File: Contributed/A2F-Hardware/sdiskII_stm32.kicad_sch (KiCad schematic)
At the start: 33 parts, among them J1 SDISKII IN (CARD), J2 SDISKII OUT (DRIVE), J3 EA W128064-OLED (FPC31), J4 UART, U1 BlackPill STMF4X1, U2 DM-OLED096-636, U3 EA OLEDM128-6, U4 74x257

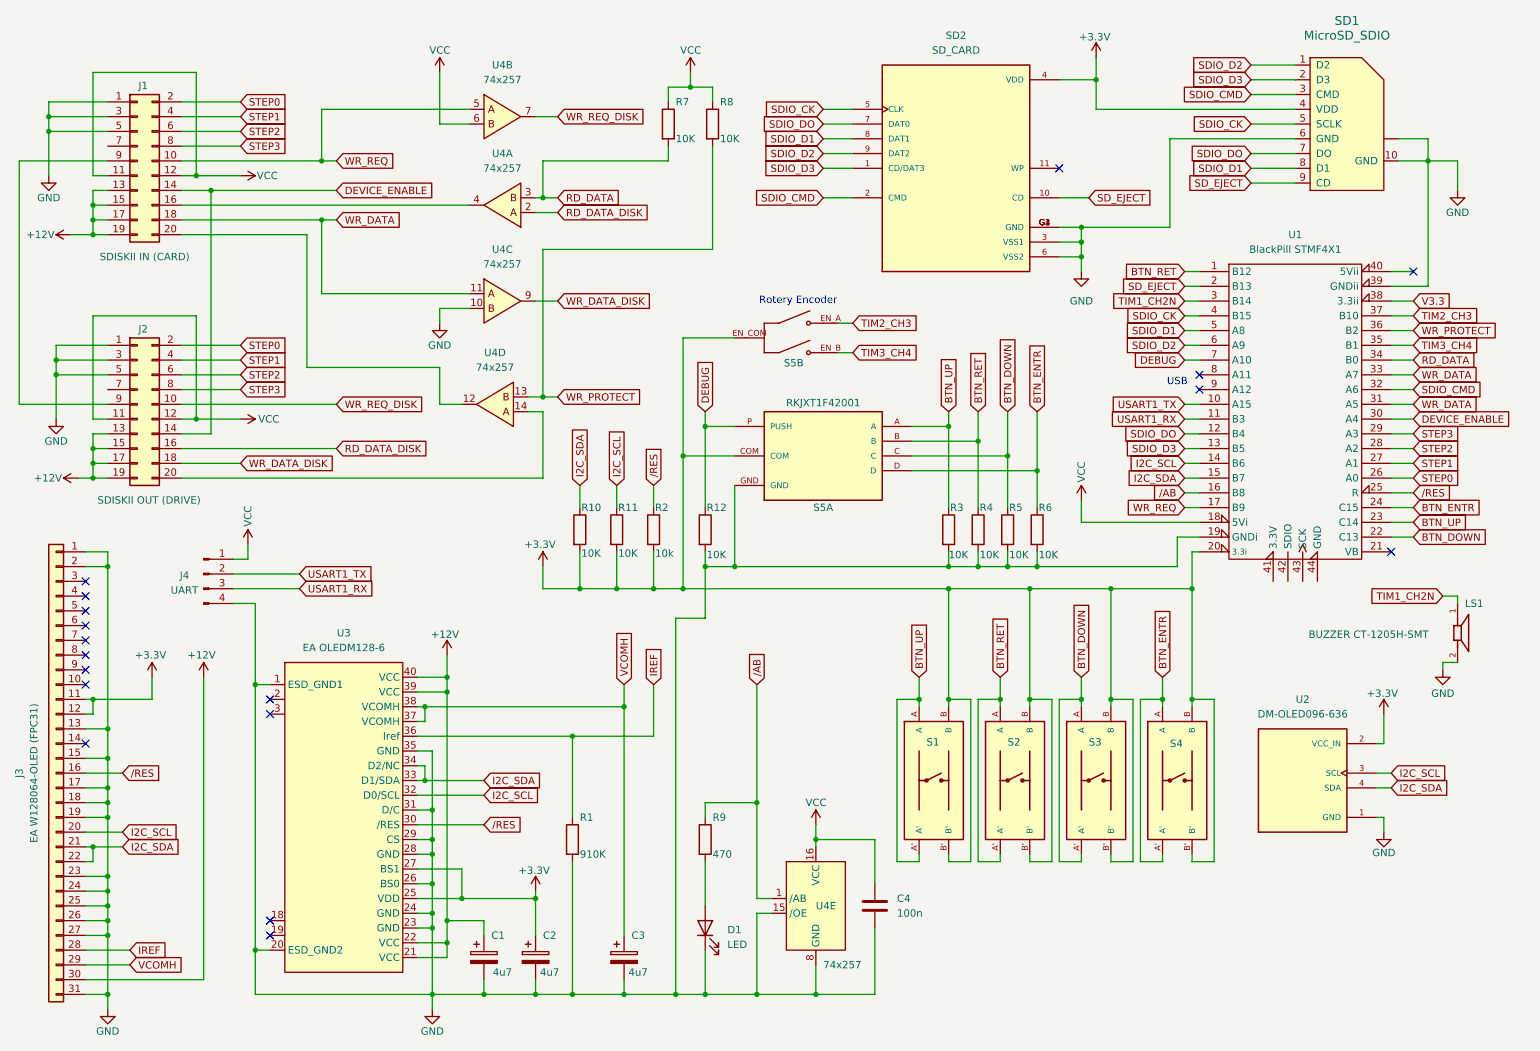
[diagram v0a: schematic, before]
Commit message: Initial upload
Rotary encoder support buggy
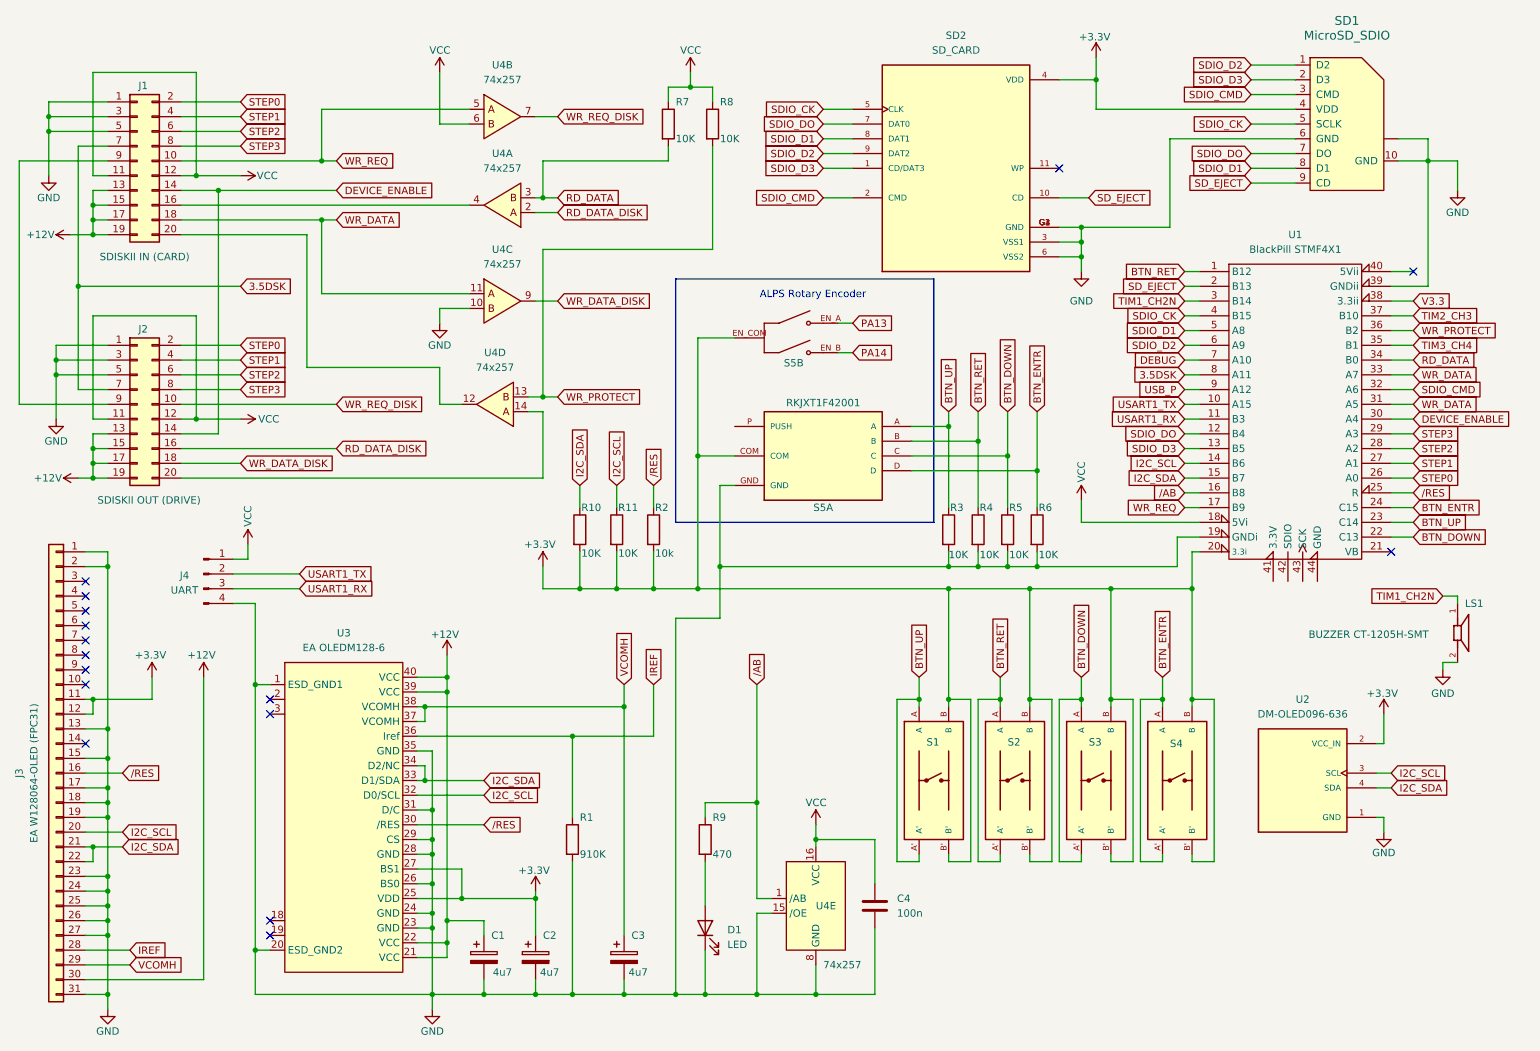
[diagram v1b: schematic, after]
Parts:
- removed R12: 10K, Resistor_SMD:R_0805_2012Metric_Pad1.20x1.40mm_HandSolder, symbol Device:R
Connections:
- net DEBUG: no longer S5.P (PUSH)
- net TIM2_CH3: no longer S5.EN_A
- net TIM3_CH4: no longer S5.EN_B
- net 3.5DSK: now reaches J1.7 (Pin_7)
- net 3.5DSK: now also J2.7 (Pin_7), U1.8 (A11)
- net USB_P: now reaches U1.9 (A12)
- new net PA13: S5.EN_A
- new net PA14: S5.EN_B
- no-connect marks 18 -> 16
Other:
- note added: "ALPS Rotary Encoder"
- note removed: "Rotery Encoder"
- note removed: "USB"

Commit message: RE update
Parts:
- added R12, R13: 10K, Resistor_SMD:R_0805_2012Metric_Pad1.20x1.40mm_HandSolder, symbol Device:R
- LS1: value BUZZER CT-1205H-SMT -> CT-1205H-SMT
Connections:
- net GND: now also R12.2, R13.2
- net PA13: now also U1.42 (SDIO), R12.1
- net PA14: now also U1.43 (SCK), R13.1
- no-connect marks 16 -> 18
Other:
- moved on the sheet: LS1

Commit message: Make Filsystem fixed
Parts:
- U1: footprint acheron_Hardware.pretty-master:Mini_F4X1_STM32_VIB -> sdisk_stm32:Mini_F4X1_STM32_VIB
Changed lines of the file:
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@@
 (kicad_sch
-	(version 20231120)
+	(version 20250114)
 	(generator "eeschema")
-	(generator_version "8.0")
+	(generator_version "9.0")
 	(paper "A4")
 	(title_block
@@
 		(rev "20")
 	)
+	(rectangle
+		(start 132.08 60.96)
+		(end 176.53 102.87)
+		(stroke
+			(width 0)
+			(type default)
+		)
+		(fill
+			(type none)
+		)
+	)
+	(text "ALPS Rotary Encoder"
+		(exclude_from_sim no)
+		(at 155.702 63.754 0)
+		(effects
+			(font
+				(size 1.27 1.27)
+			)
+		)
+	)
 	(junction
 		(at 207.01 114.3)
@@
 		)
 	)
-	(rectangle
-		(start 132.08 60.96)
-		(end 176.53 102.87)
-		(stroke
-			(width 0)
-			(type default)
-		)
-		(fill
-			(type none)
-		)
-	)
-	(text "ALPS Rotary Encoder"
-		(exclude_from_sim no)
-		(at 155.702 63.754 0)
-		(effects
-			(font
-				(size 1.27 1.27)
-			)
-		)
-	)
 	(global_label "USART1_RX"
 		(shape input)
@@
 			)
 		)
-		(property "Footprint" "acheron_Hardware.pretty-master:Mini_F4X1_STM32_VIB"
+		(property "Footprint" "sdisk_stm32:Mini_F4X1_STM32_VIB"
 			(at 240.792 127.254 0)
 			(effects
@@
 		)
 	)
+	(embedded_fonts no)
 )

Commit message: final v0.80.1
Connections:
- net BTN_ENTR: now also S5.P (PUSH)
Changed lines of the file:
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@@
 	)
 	(rectangle
-		(start 132.08 60.96)
-		(end 176.53 102.87)
+		(start 133.35 60.96)
+		(end 176.53 104.14)
 		(stroke
 			(width 0)
@@
 	)
 	(junction
+		(at 138.43 110.49)
+		(diameter 0)
+		(color 0 0 0 0)
+	)
+	(junction
 		(at 90.17 152.4)
 		(diameter 0)
@@
 	)
 	(junction
+		(at 173.99 93.98)
+		(diameter 0)
+		(color 0 0 0 0)
+	)
+	(junction
 		(at 31.75 50.8)
 		(diameter 0)
@@
 	)
 	(junction
-		(at 139.7 110.49)
-		(diameter 0)
-		(color 0 0 0 0)
-	)
-	(junction
 		(at 31.75 95.25)
 		(diameter 0)
@@
 	(wire
 		(pts
+			(xy 138.43 110.49) (xy 179.07 110.49)
+		)
+		(stroke
+			(width 0)
+			(type default)
+		)
+	)
+	(wire
+		(pts
 			(xy 179.07 161.29) (xy 179.07 160.02)
 		)
@@
 	(wire
 		(pts
-			(xy 139.7 96.52) (xy 142.24 96.52)
+			(xy 138.43 96.52) (xy 142.24 96.52)
 		)
 		(stroke
@@
 	(wire
 		(pts
-			(xy 172.72 93.98) (xy 194.31 93.98)
+			(xy 173.99 93.98) (xy 194.31 93.98)
+		)
+		(stroke
+			(width 0)
+			(type default)
+		)
+	)
+	(wire
+		(pts
+			(xy 172.72 93.98) (xy 173.99 93.98)
 		)
 		(stroke
@@
 	(wire
 		(pts
-			(xy 139.7 96.52) (xy 139.7 110.49)
+			(xy 138.43 96.52) (xy 138.43 110.49)
 		)
 		(stroke
@@
 	(wire
 		(pts
+			(xy 140.97 86.36) (xy 140.97 101.6)
+		)
+		(stroke
+			(width 0)
+			(type default)
+		)
+	)
+	(wire
+		(pts
 			(xy 255.27 90.17) (xy 259.08 90.17)
 		)
@@
 	(wire
 		(pts
-			(xy 215.9 133.35) (xy 215.9 134.62)
+			(xy 140.97 101.6) (xy 173.99 101.6)
 		)
 		(stroke
@@
 	(wire
 		(pts
-			(xy 220.98 107.95) (xy 220.98 114.3)
+			(xy 215.9 133.35) (xy 215.9 134.62)
 		)
 		(stroke
@@
 	(wire
 		(pts
-			(xy 31.75 87.63) (xy 31.75 90.17)
+			(xy 220.98 107.95) (xy 220.98 114.3)
 		)
 		(stroke
@@
 	(wire
 		(pts
-			(xy 139.7 110.49) (xy 179.07 110.49)
+			(xy 31.75 87.63) (xy 31.75 90.17)
 		)
 		(stroke
@@
 	(wire
 		(pts
+			(xy 173.99 93.98) (xy 173.99 101.6)
+		)
+		(stroke
+			(width 0)
+			(type default)
+		)
+	)
+	(wire
+		(pts
 			(xy 109.22 114.3) (xy 109.22 110.49)
 		)
@@
 	(wire
 		(pts
-			(xy 132.08 119.38) (xy 139.7 119.38)
+			(xy 132.08 119.38) (xy 138.43 119.38)
 		)
 		(stroke
@@
 	(wire
 		(pts
-			(xy 139.7 110.49) (xy 139.7 119.38)
+			(xy 138.43 110.49) (xy 138.43 119.38)
 		)
 		(stroke
@@
 		)
 		(stroke
+			(width 0)
+			(type default)
+		)
+	)
+	(wire
+		(pts
+			(xy 142.24 86.36) (xy 140.97 86.36)
+		)
+		(stroke
